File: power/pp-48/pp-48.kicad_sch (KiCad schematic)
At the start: 0 parts

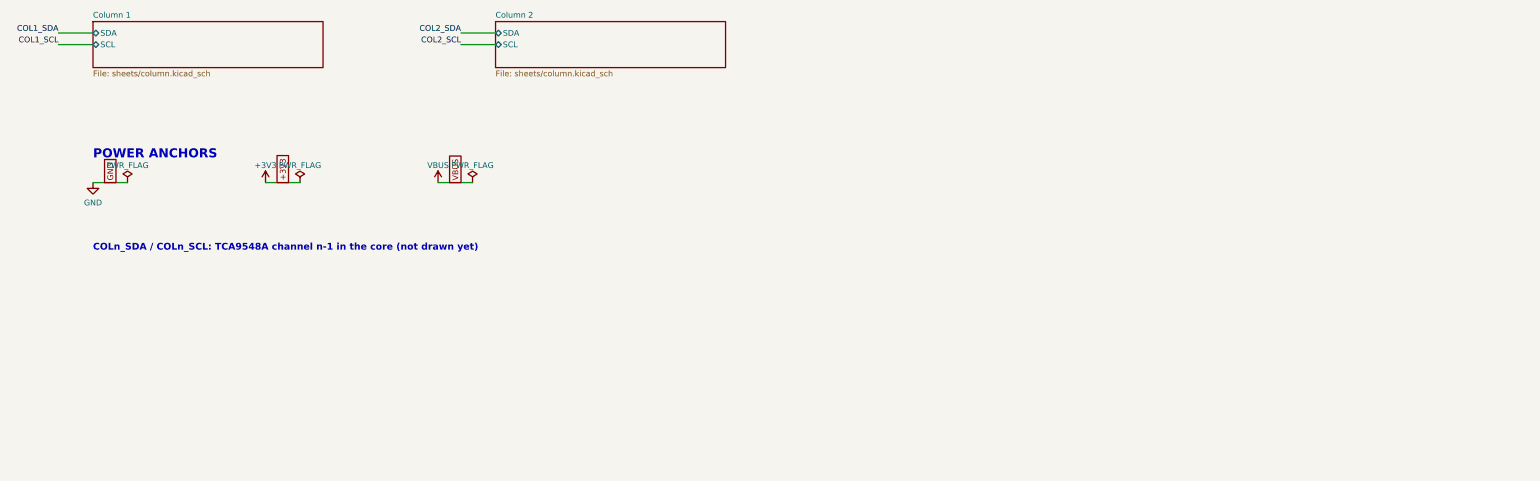
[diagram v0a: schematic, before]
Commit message: pp-48: core sheets MCU (PP-48-2S MCU cut down to link slave + mux master, tile hot-swap GPIO, VIN_SNS), Mux (TCA9548A, channel k = column k+1), Link (as PP-48-2S), Supplies (LM5164 3V3 from VIN); input sheet and isolated 12 V aux pending parts; handoff
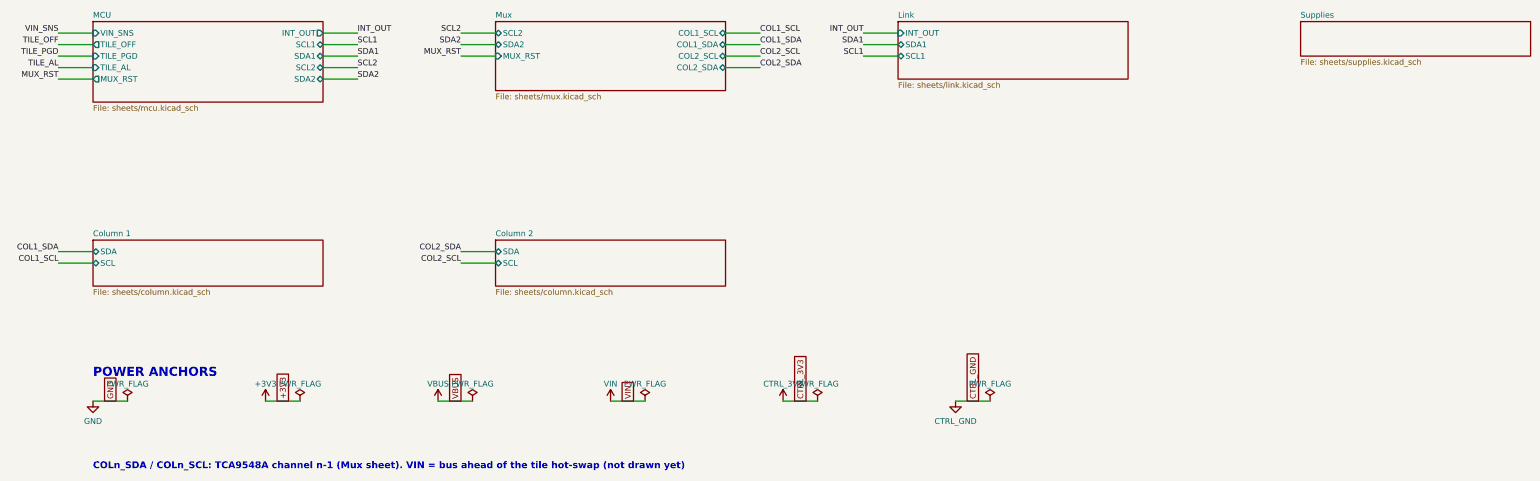
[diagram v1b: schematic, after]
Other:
- added sheet Link (sheets/link.kicad_sch)
- added sheet MCU (sheets/mcu.kicad_sch)
- added sheet Mux (sheets/mux.kicad_sch)
- added sheet Supplies (sheets/supplies.kicad_sch)
- note added: "COLn_SDA / COLn_SCL: TCA9548A channel n-1 (Mux sheet). VIN = bus ahead of the tile hot-swap (not drawn yet)"
- note removed: "COLn_SDA / COLn_SCL: TCA9548A channel n-1 in the core (not drawn yet)"

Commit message: pp-48: Supplies sheet gets the isolated 12 V aux as an INTERIM off-the-shelf module (U2 URB4812YMD-6WR3 class, 6 W, 1.5 kV, LCSC C5369743; Cin 22u + 2.2u 100V, Cout 10u, LED, J4 JST PH CTRL_12V / CTRL_GND), standing in for the own Fly-Buck until an isolated coupled inductor is found at LCSC; pp:DCDC_Iso_1x1_Single symbol and pp48:Converter_DCDC_1x1in_THT footprint; ERC only the input-sheet labels; ADR 0003 decision 14 and handoff note the revisit
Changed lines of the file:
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@@
 		(comment 1 "48 V plane, 2 identical columns: LM5069-2 + INA238 + TCA9535 + ID ADC per column, screwed PM-19V-250W module")
 		(comment 2 "generated by tools/gensch.py; docs/adr/0004-plane-column-layout.md, 0003, 0002")
-		(comment 3 "core: MCU, mux, link, 3V3; tile hot-swap, isolated 12 V aux and end cap not drawn yet")
+		(comment 3 "core: MCU, mux, link, 3V3, isolated 12 V (interim module); tile hot-swap and end cap not drawn yet")
 	)
 	(sheet
@@
 	(wire
 		(pts
-			(xy 228.6 121.92) (xy 236.22 121.92)
+			(xy 228.6 121.92) (xy 232.41 121.92)
 		)
 		(stroke
@@
 	)
 	(symbol
-		(lib_id "power:PWR_FLAG")
-		(at 236.22 121.92 0)
+		(lib_id "power:+12V")
+		(at 266.7 121.92 0)
 		(unit 1)
 		(body_style 1)
@@
 		(in_pos_files yes)
 		(dnp no)
-		(property "Reference" "#FLG9012"
-			(at 236.22 121.92 0)
-			(hide yes)
-			(show_name no)
-			(do_not_autoplace no)
-			(effects
-				(font
-					(size 1.27 1.27)
-				)
-			)
-		)
-		(property "Value" "PWR_FLAG"
-			(at 236.22 118.11 0)
+		(property "Reference" "#PWR9012"
+			(at 266.7 121.92 0)
+			(hide yes)
+			(show_name no)
+			(do_not_autoplace no)
+			(effects
+				(font
+					(size 1.27 1.27)
+				)
+			)
+		)
+		(property "Value" "CTRL_12V"
+			(at 266.7 118.11 0)
 			(show_name no)
 			(do_not_autoplace no)
@@
 		)
 		(property "Footprint" ""
-			(at 236.22 121.92 0)
+			(at 266.7 121.92 0)
 			(hide yes)
 			(show_name no)
@@
 		)
 		(property "Datasheet" ""
-			(at 236.22 121.92 0)
+			(at 266.7 121.92 0)
 			(hide yes)
 			(show_name no)
@@
 		)
 		(property "Description" ""
-			(at 236.22 121.92 0)
+			(at 266.7 121.92 0)
 			(hide yes)
 			(show_name no)
@@
 			(project "pp-48"
 				(path "/cf0d5c0a-6642-53ea-ac93-0bbad631a43a"
-					(reference "#FLG9012")
+					(reference "#PWR9012")
 					(unit 1)
 				)
 			)
+		)
+	)
+	(wire
+		(pts
+			(xy 266.7 121.92) (xy 270.51 121.92)
+		)
+		(stroke
+			(width 0)
+			(type default)
+		)
+	)
+	(global_label "CTRL_12V"
+		(shape passive)
+		(at 270.51 121.92 90)
+		(fields_autoplaced yes)
+		(effects
+			(font
+				(size 1.27 1.27)
+			)
+			(justify left)
+		)
+		(property "Intersheetrefs" "${INTERSHEET_REFS}"
+			(at 270.51 121.92 0)
+			(show_name no)
+			(do_not_autoplace no)
+			(hide yes)
+			(effects
+				(font
+					(size 1.27 1.27)
+				)
+			)

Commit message: pp-48: Input sheet (J1 XT90PW-M, D1 SMDJ60A bus TVS, C1 / C2 input caps, tile hot-swap U7 LM5069MM-1 latch-off with 2 x 4 mOhm shunt = 2 mOhm (limit 27.5 A, under the XT90's 30 A), Q2 || Q3 BSC040N10NS5 with own gate resistors, power limit ~75 W, UVLO / OVLO / timer as the columns, Q4 TILE_OFF on UVLO, TILE_PGD; U8 INA238 0x40 on I2C2 with TILE_AL; VIN_SNS divider); sheet order Input, Supplies, MCU, Mux, Link; ERC 0; ADR 0003 tile values, handoff with parts to check
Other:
- added sheet Input (sheets/input.kicad_sch)
- note added: "COLn_SDA / COLn_SCL: TCA9548A channel n-1 (Mux sheet). VIN = bus ahead of the tile hot-swap (Input sheet)"
- note removed: "COLn_SDA / COLn_SCL: TCA9548A channel n-1 (Mux sheet). VIN = bus ahead of the tile hot-swap (not drawn yet)"

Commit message: pp-48: schematic as 2-slot units (ADR 0004 decision 9): sheets/unit.kicad_sch replaces column.kicad_sch, instantiated N/2 times (refs +100 per unit, slot B +50, nets A_* / B_*); TCA6424ARGJR U5 (0x22, LCSC C80692, pp symbol added, VQFN-32 EP3.15) with C9 / C13 / R30 and the segment pull-ups once per unit; slot B straps INA238 A0 and ADC ADR0 to +3V3 (0x41 / 0x52); root nets UNITu_SDA / SCL, mux channel k = unit k+1; ERC 0
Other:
- removed sheet Column 1
- removed sheet Column 2
- added sheet Unit 1 (sheets/unit.kicad_sch)
- sheet Mux ports: added UNIT1_SCL, UNIT1_SDA; removed COL1_SCL, COL1_SDA, COL2_SCL, COL2_SDA
- note added: "UNITu_SDA / UNITu_SCL: TCA9548A channel u-1 (Mux sheet). VIN = bus ahead of the tile hot-swap (Input sheet)"
- note removed: "COLn_SDA / COLn_SCL: TCA9548A channel n-1 (Mux sheet). VIN = bus ahead of the tile hot-swap (Input sheet)"
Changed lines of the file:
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@@
 		(rev "0.1")
 		(company "Granite")
-		(comment 1 "48 V plane, 2 identical columns: LM5069-2 + INA238 + TCA9535 + ID ADC per column, screwed PM-19V-250W module")
+		(comment 1 "48 V plane, 2 slots in 1 units: LM5069-2 + INA238 + ID ADC per slot, TCA6424A per unit, screwed PM-19V-250W module")
 		(comment 2 "generated by tools/gensch.py; docs/adr/0004-plane-column-layout.md, 0003, 0002")
 		(comment 3 "core: tile input (XT90, LM5069-1 hot-swap), supplies, MCU, mux, link; end cap (N = 6/8) not drawn yet")
@@
 	(sheet
 		(at 304.8 38.1)
-		(size 50.8 15.24)
+		(size 50.8 12.7)
 		(exclude_from_sim no)
 		(in_bom yes)
@@
 		)
 		(property "Sheetfile" "sheets/mux.kicad_sch"
-			(at 304.8 53.9284 0)
+			(at 304.8 51.3884 0)
 			(show_name no)
 			(do_not_autoplace no)
@@
 			)
 		)
-		(pin "COL1_SCL" bidirectional
+		(pin "UNIT1_SCL" bidirectional
 			(at 355.6 40.64 0)
 			(effects
@@
 			)
 		)
-		(pin "COL1_SDA" bidirectional
+		(pin "UNIT1_SDA" bidirectional
 			(at 355.6 43.18 0)
-			(effects
-				(font
-					(size 1.27 1.27)
-				)
-				(justify right)
-			)
-		)
-		(pin "COL2_SCL" bidirectional
-			(at 355.6 45.72 0)
-			(effects
-				(font
-					(size 1.27 1.27)
-				)
-				(justify right)
-			)
-		)
-		(pin "COL2_SDA" bidirectional
-			(at 355.6 48.26 0)
 			(effects
 				(font
@@
 		)
 	)
-	(label "COL1_SCL"
+	(label "UNIT1_SCL"
 		(at 363.22 40.64 0)
 		(effects
@@
 		)
 	)
-	(label "COL1_SDA"
+	(label "UNIT1_SDA"
 		(at 363.22 43.18 0)
-		(effects
-			(font
-				(size 1.27 1.27)
-			)
-			(justify left bottom)
-		)
-	)
-	(wire
-		(pts
-			(xy 355.6 45.72) (xy 363.22 45.72)
-		)
-		(stroke
-			(width 0)
-			(type default)
-		)
-	)
-	(label "COL2_SCL"
-		(at 363.22 45.72 0)
-		(effects
-			(font
-				(size 1.27 1.27)
-			)
-			(justify left bottom)
-		)
-	)
-	(wire
-		(pts
-			(xy 355.6 48.26) (xy 363.22 48.26)
-		)
-		(stroke
-			(width 0)
-			(type default)
-		)
-	)
-	(label "COL2_SDA"
-		(at 363.22 48.26 0)
 		(effects
 			(font
@@
 			(color 0 0 0 0)
 		)
-		(property "Sheetname" "Column 1"
+		(property "Sheetname" "Unit 1"
 			(at 38.1 85.6484 0)
 			(show_name no)
@@
 			)
 		)
-		(property "Sheetfile" "sheets/column.kicad_sch"
+		(property "Sheetfile" "sheets/unit.kicad_sch"
 			(at 38.1 97.1084 0)
 			(show_name no)
@@
 		)
 	)
-	(label "COL1_SDA"
+	(label "UNIT1_SDA"
 		(at 30.48 88.9 180)
 		(effects
@@
 		)
 	)
-	(label "COL1_SCL"
+	(label "UNIT1_SCL"
 		(at 30.48 91.44 180)
-		(effects
-			(font
-				(size 1.27 1.27)
-			)
-			(justify right bottom)
-		)
-	)
-	(sheet
-		(at 127 86.36)
-		(size 50.8 10.16)
-		(exclude_from_sim no)
-		(in_bom yes)
-		(on_board yes)
-		(dnp no)
-		(fields_autoplaced yes)
-		(stroke
-			(width 0.1524)
-			(type solid)
-		)
-		(fill
-			(color 0 0 0 0)
-		)
-		(property "Sheetname" "Column 2"
-			(at 127 85.6484 0)
-			(show_name no)
-			(do_not_autoplace no)
-			(effects
-				(font
-					(size 1.27 1.27)
-				)
-				(justify left bottom)
-			)
-		)
-		(property "Sheetfile" "sheets/column.kicad_sch"
-			(at 127 97.1084 0)
-			(show_name no)
-			(do_not_autoplace no)
-			(effects
-				(font
-					(size 1.27 1.27)
-				)
-				(justify left top)
-			)
-		)
-		(pin "SDA" bidirectional
-			(at 127 88.9 180)
-			(effects
-				(font
-					(size 1.27 1.27)
-				)
-				(justify left)
-			)
-		)
-		(pin "SCL" bidirectional
-			(at 127 91.44 180)
-			(effects
-				(font
-					(size 1.27 1.27)
-				)
-				(justify left)
-			)
-		)
-		(instances
-			(project "pp-48"
-				(path "/cf0d5c0a-6642-53ea-ac93-0bbad631a43a"
-					(page "8")
-				)
-			)
-		)
-	)
-	(wire
-		(pts
-			(xy 127 88.9) (xy 119.38 88.9)
-		)
-		(stroke
-			(width 0)
-			(type default)
-		)
-	)
-	(label "COL2_SDA"
-		(at 119.38 88.9 180)
-		(effects
-			(font
-				(size 1.27 1.27)
-			)
-			(justify right bottom)
-		)
-	)
-	(wire
-		(pts
-			(xy 127 91.44) (xy 119.38 91.44)
-		)
-		(stroke
-			(width 0)
-			(type default)
-		)
-	)
-	(label "COL2_SCL"
-		(at 119.38 91.44 180)
 		(effects
 			(font
@@
 		)
 	)
-	(text "COLn_SDA / COLn_SCL: TCA9548A channel n-1 (Mux sheet). VIN = bus ahead of the tile hot-swap (Input sheet)"
+	(text "UNITu_SDA / UNITu_SCL: TCA9548A channel u-1 (Mux sheet). VIN = bus ahead of the tile hot-swap (Input sheet)"
 		(exclude_from_sim no)
 		(at 38.1 137.16 0)
